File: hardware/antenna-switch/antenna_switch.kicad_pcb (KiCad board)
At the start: 4 copper layers, 45.2 x 53.3 mm, 32 parts, among them J8 Conn_01x04, U40 SN74LVC2G14, U41 HMC7992, U42 HMC7992

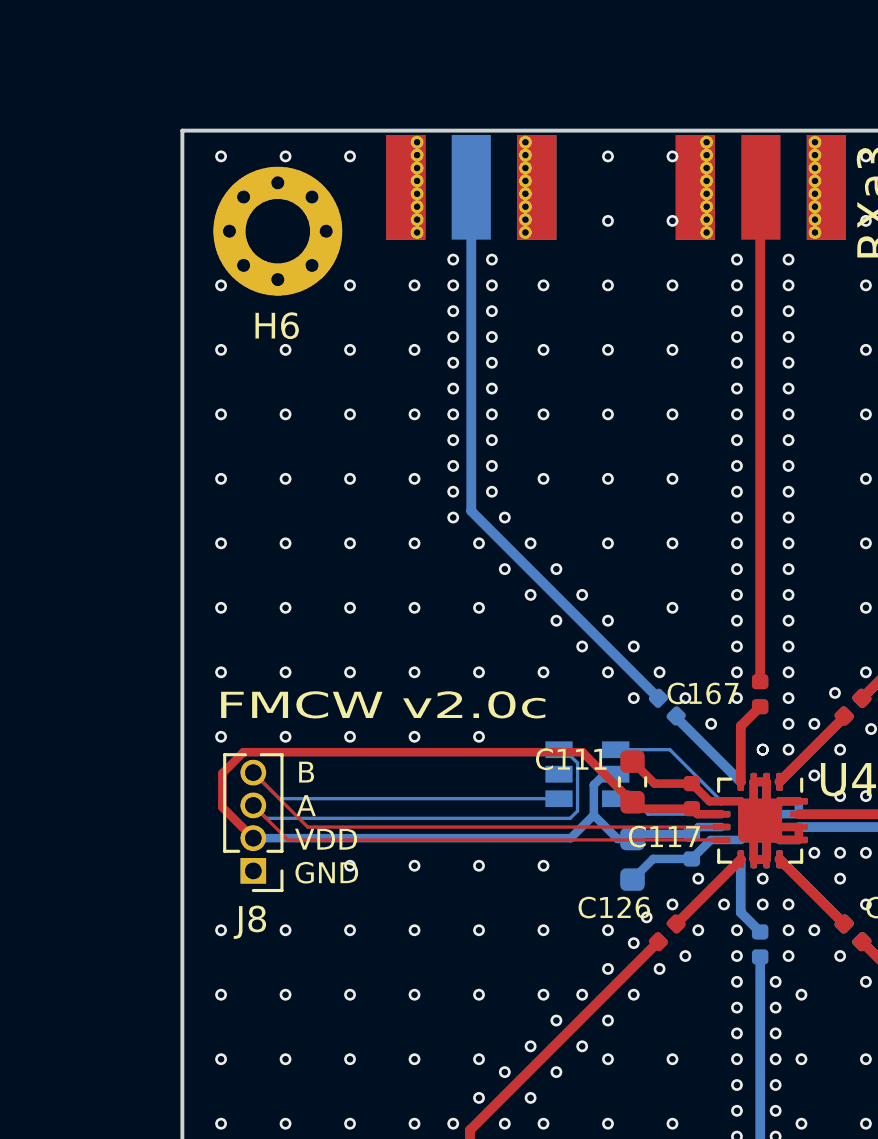
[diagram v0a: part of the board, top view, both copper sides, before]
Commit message: Huge, messy commit before I begin replacing FPGA code
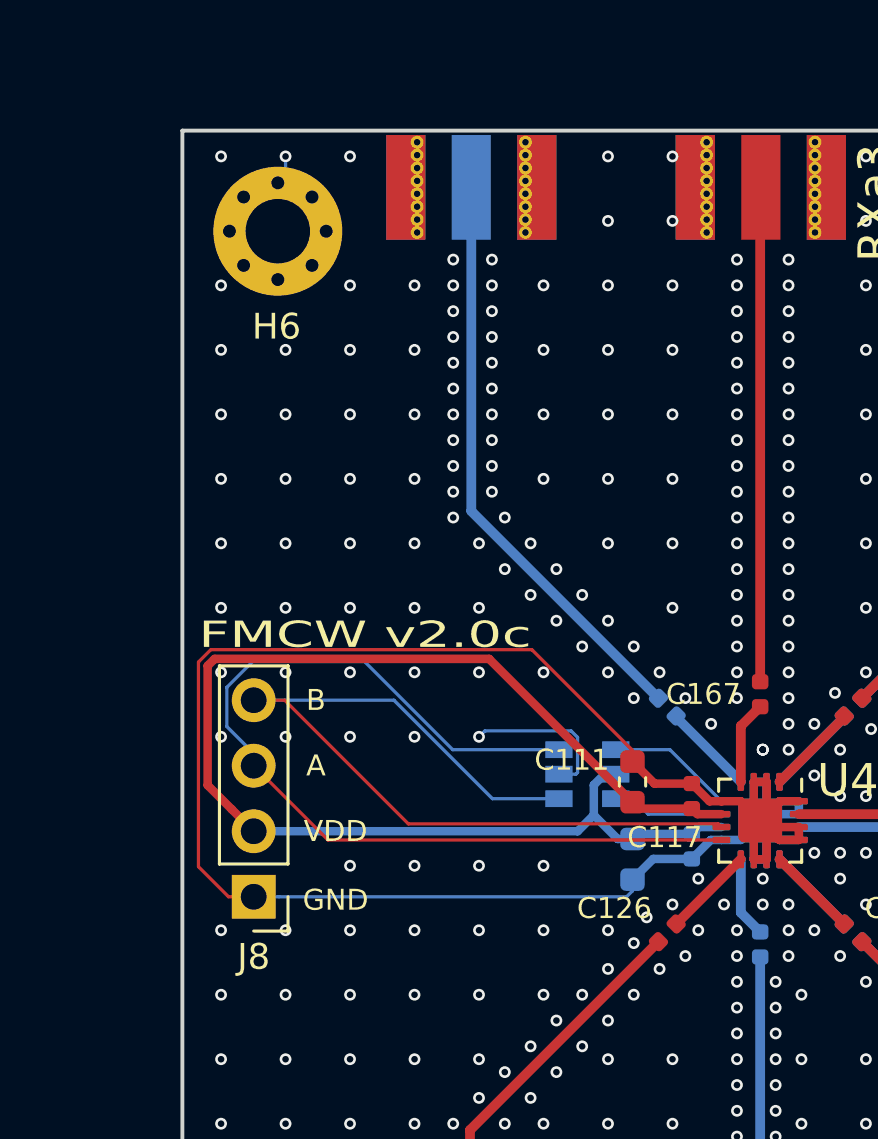
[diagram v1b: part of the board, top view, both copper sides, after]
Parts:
- J8: footprint Connector_PinHeader_1.27mm:PinHeader_1x04_P1.27mm_Vertical -> Connector_PinHeader_2.54mm:PinHeader_1x04_P2.54mm_Vertical
- moved J8 1.00 mm to (210.8, 118.8)
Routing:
- net GND: track 37.4 -> 91.4 mm
- net VDD: track 45.0 -> 50.8 mm
- net /RF Switch/A: track 34.4 -> 37.5 mm
- net /RF Switch/B: track 31.3 -> 33.6 mm
